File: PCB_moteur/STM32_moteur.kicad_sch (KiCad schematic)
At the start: 54 parts, among them U1 STM32F103CBT6

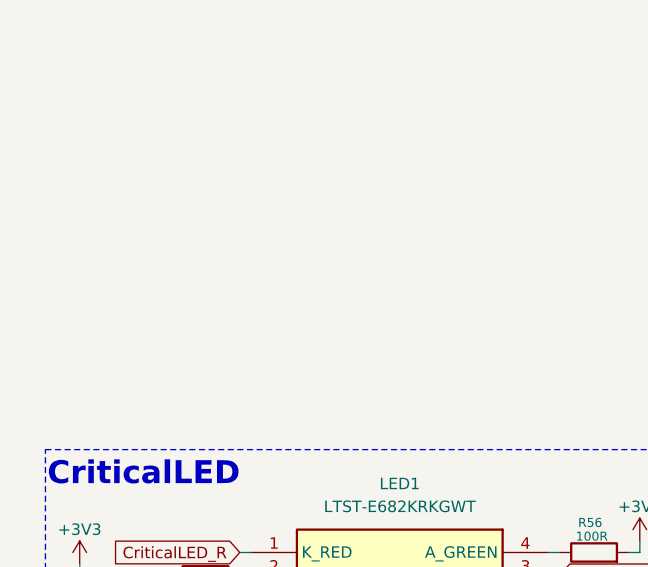
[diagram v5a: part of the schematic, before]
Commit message: Added LDO, INA125, sensors
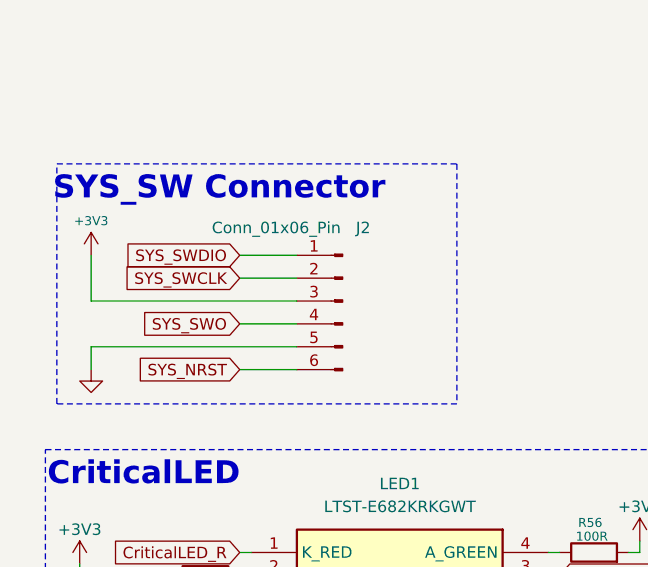
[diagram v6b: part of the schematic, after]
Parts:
- added J2: Conn_01x06_Pin, symbol Connector:Conn_01x06_Pin
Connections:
- net +3V3: now also J2.3 (Pin_3), J2.6 (Pin_6)
- net GND: now also J2.5 (Pin_5)
- net SYS_SWCLK: now also J2.2 (Pin_2)
- net SYS_SWDIO: now also J2.1 (Pin_1)
- new net SYS_SWO: J2.4 (Pin_4)
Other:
- note added: "SYS_SW Connector"
